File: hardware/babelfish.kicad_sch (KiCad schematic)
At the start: 103 parts, among them J1 Shifter Power, J2 SWD, J3 DE9 Female, J4 USB_A, Q1 BSS138, SW1 TS342A2P-WZ, SW2 TS342A2P-WZ, U1 RP2040, U10 DSWB04LHGET, U11 MAX3232IDR, U12 AP2191WG-7, U2 TPS2113ADRBR, U3 GT-USB-7010ASV, U4 W25Q128JVS, U6 TPMCP1703T-3302E_CB, U7 74HC4052PW,118, U8 74HC4052PW,118, U9 LMR14020SDDAR, X1 X322512MSB4SI

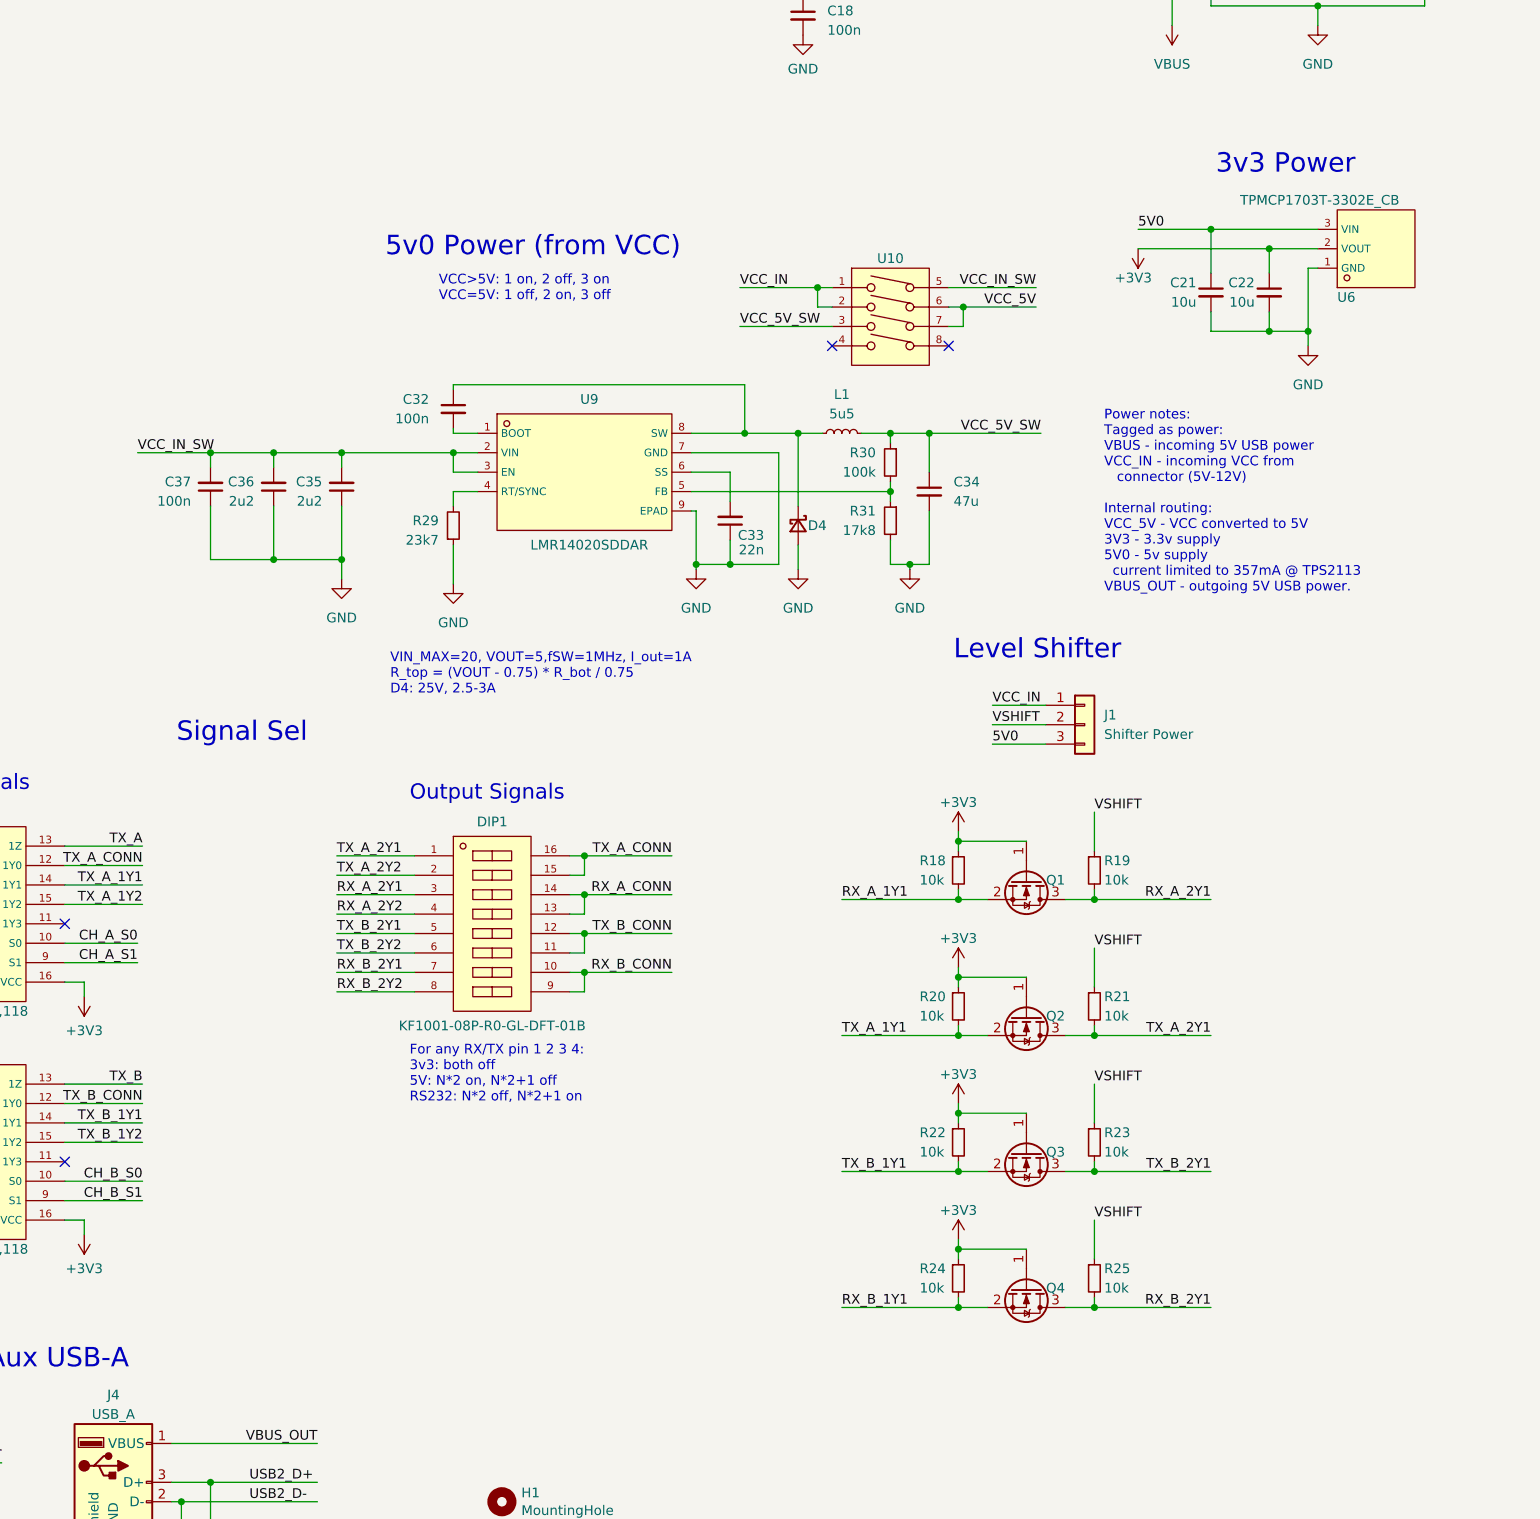
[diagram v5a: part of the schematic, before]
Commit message: Move 5V power to TPS62933, from WEBENCH
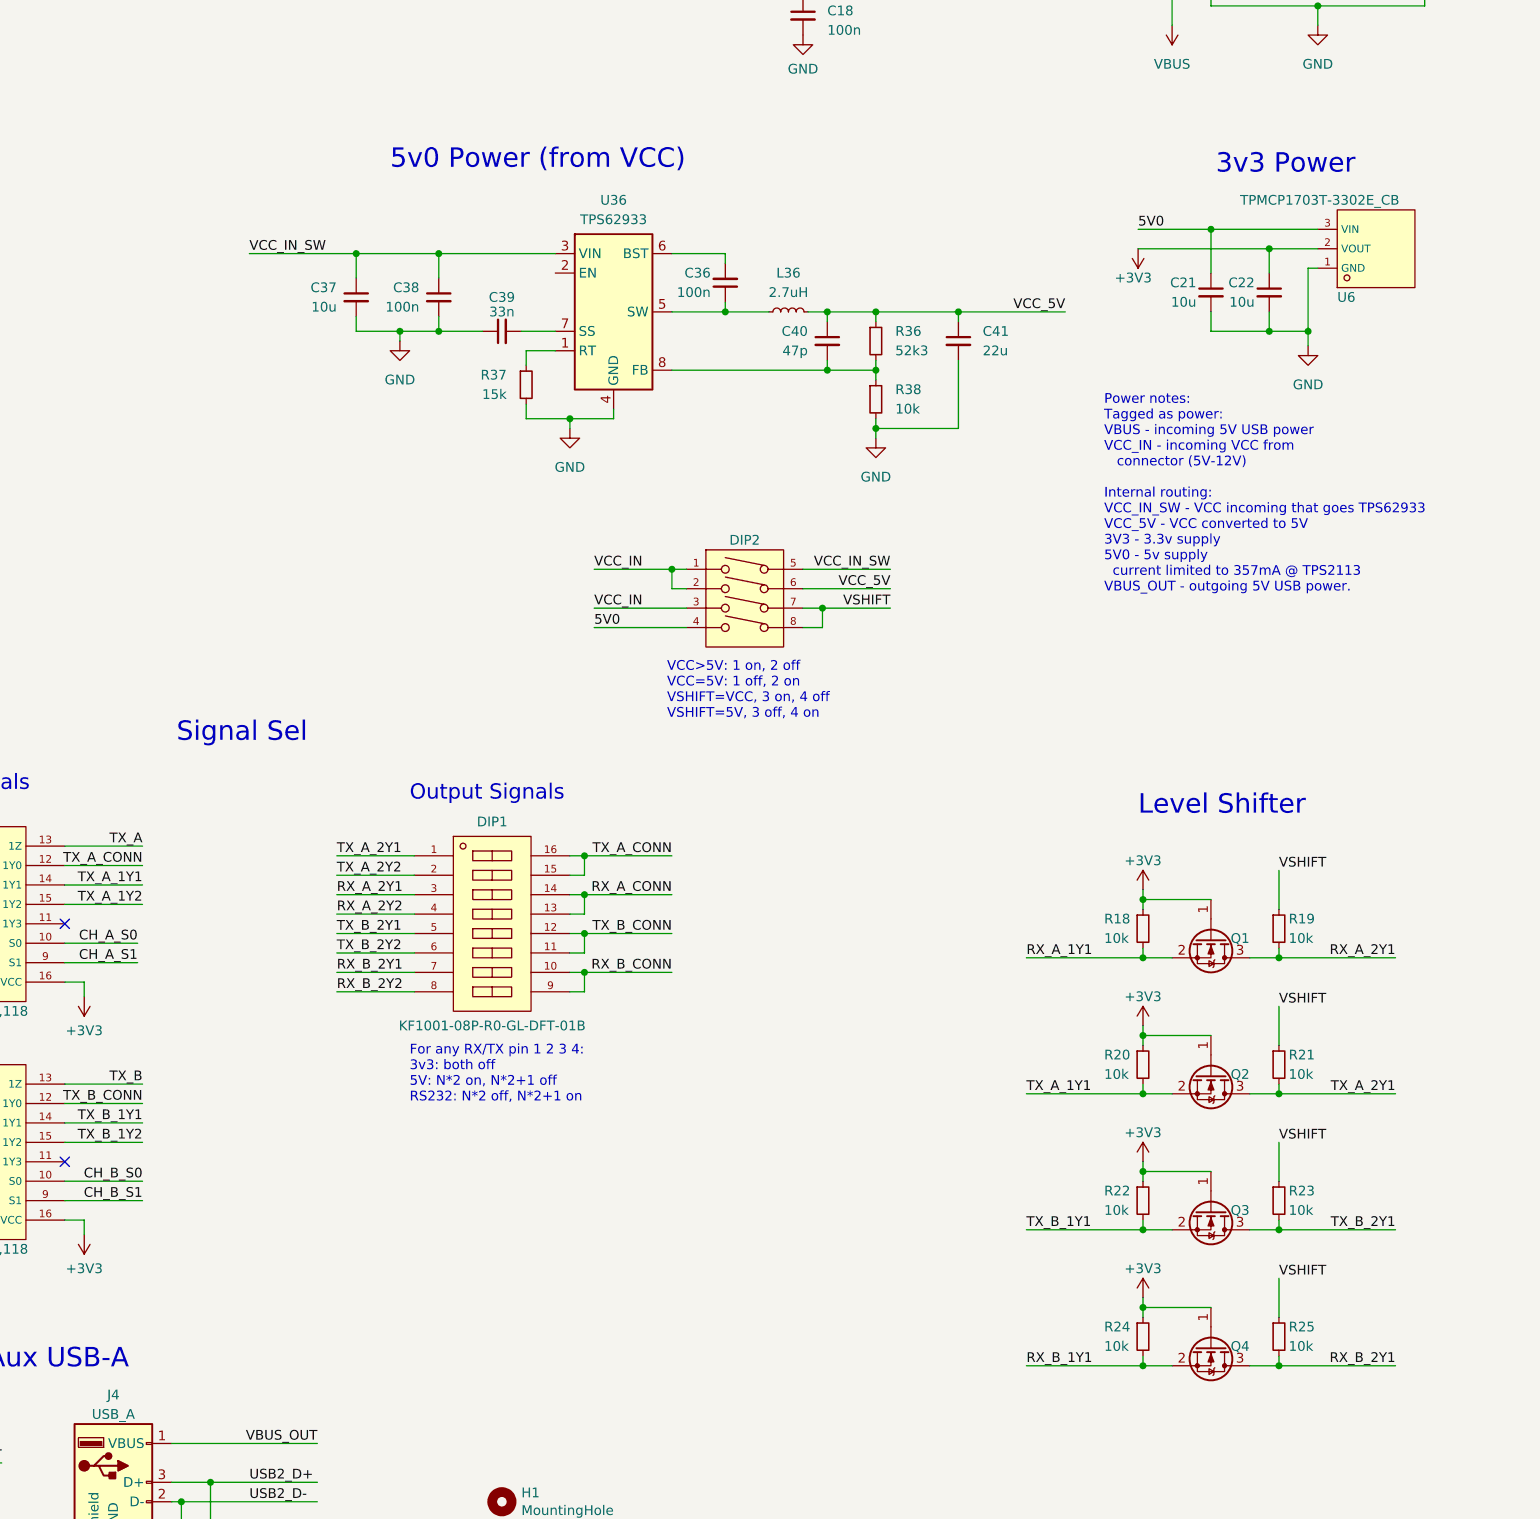
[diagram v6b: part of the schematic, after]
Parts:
- removed C32: 100n, Capacitor_SMD:C_0402_1005Metric, symbol Device:C_Small
- removed C33: 22n, Capacitor_SMD:C_0402_1005Metric, symbol Device:C_Small
- removed C34: 47u, Capacitor_SMD:C_0805_2012Metric, symbol Device:C_Small
- removed C35: 2u2, Capacitor_SMD:C_1206_3216Metric, symbol Device:C_Small
- removed D4: D_Schottky_Small, Diode_SMD:D_SMA, symbol Device:D_Schottky_Small
- removed J1: Shifter Power, Connector_PinHeader_2.54mm:PinHeader_1x03_P2.54mm_Vertical, symbol Connector_Generic:Conn_01x03
- removed L1: 5u5, symbol Device:L_Small
- removed R29: 23k7, symbol Device:R_Small
- removed R30: 100k, symbol Device:R_Small
- removed R31: 17k8, symbol Device:R_Small
- removed U9: LMR14020SDDAR, lcsc:HSOP-8_L5.0-W4.0-P1.27-LS6.2-BL-EP, symbol LCSC:LMR14020SDDAR
- added C38: 100n, Capacitor_SMD:C_0402_1005Metric, symbol Device:C_Small
- added C39: 33n, Capacitor_SMD:C_01005_0402Metric, symbol Device:C_Small
- added C40: 47p, Capacitor_SMD:C_0402_1005Metric, symbol Device:C_Small
- added C41: 22u, Capacitor_SMD:C_0805_2012Metric, symbol Device:C_Small
- added L36: 2.7uH, Inductor_SMD:L_12x12mm_H6mm, symbol Device:L_Small
- added R36: 52k3, Resistor_SMD:R_0402_1005Metric, symbol Device:R_Small
- added R37: 15k, Resistor_SMD:R_0402_1005Metric, symbol Device:R_Small
- added R38: 10k, Resistor_SMD:R_0402_1005Metric, symbol Device:R_Small
- added U36: TPS62933, Package_TO_SOT_SMD:SOT-583-8, symbol Regulator_Switching:TPS62933
- C36: value 2u2 -> 100n; footprint Capacitor_SMD:C_1206_3216Metric -> Capacitor_SMD:C_01005_0402Metric; ESR (none) -> 1mOhm; Notes X7R 100V -> (none)
- C37: value 100n -> 10u; footprint Capacitor_SMD:C_0402_1005Metric -> Capacitor_SMD:C_0805_2012Metric; ESR (none) -> 2.8mOhm; Notes X7R 100V -> (none)
- renumbered U10 to DIP2
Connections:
- net VCC_5V_SW is gone; now on net VCC_IN: DIP2.3
- net 5V0: now also DIP2.4
- net GND: now also C37.2, C38.2, C39.1, C41.2, R37.2, R38.2, U36.4 (GND); no longer C36.1, C37.1
- net VCC_5V: now also C40.1, C41.1, L36.2, R36.1; no longer DIP2.7
- net VCC_IN_SW: now also C37.1, C38.1, U36.3 (VIN); no longer C36.2, C37.2
- net VSHIFT: now also DIP2.7, DIP2.8
- new net: C40.2, R36.2, R38.1, U36.8 (FB)
- new net: R37.1, U36.1 (RT)
- new net: C36.1, L36.1, U36.5 (SW)
- new net: C39.2, U36.7 (SS)
- new net: C36.2, U36.6 (BST)
- no-connect marks 18 -> 16
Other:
- note added: "Power notes: Tagged as power: VBUS - incoming 5V USB power VCC_IN - incoming VCC from connector (5V-12V) Internal routing: VCC_IN_SW - VCC incoming that goes TPS62933 VCC_5V - VCC converted to 5V 3V3 - 3.3v supply 5V0 - 5v supply current limited to 357mA @ TPS2113 VBUS_OUT - outgoing 5V USB power."
- note added: "VCC>5V: 1 on, 2 off VCC=5V: 1 off, 2 on VSHIFT=VCC, 3 on, 4 off VSHIFT=5V, 3 off, 4 on"
- note removed: "Power notes: Tagged as power: VBUS - incoming 5V USB power VCC_IN - incoming VCC from connector (5V-12V) Internal routing: VCC_5V - VCC converted to 5V 3V3 - 3.3v supply 5V0 - 5v supply current limited to 357mA @ TPS2113 VBUS_OUT - outgoing 5V USB power."
- note removed: "VCC>5V: 1 on, 2 off, 3 on VCC=5V: 1 off, 2 on, 3 off"
- note removed: "VIN_MAX=20, VOUT=5,fSW=1MHz, I_out=1A R_top = (VOUT - 0.75) * R_bot / 0.75 D4: 25V, 2.5-3A"
- moved on the sheet: DIP2, Q1, Q2, Q3, Q4, R18, R19, R20, R21, R22, R23, R24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

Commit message: WIP -- pre-shift-up
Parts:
- L36: footprint Inductor_SMD:L_12x12mm_H6mm -> lcsc:IND-SMD_L6.0-W6.0_FNR60XXS
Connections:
- no-connect marks 16 -> 17
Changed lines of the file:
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@@
   (no_connect (at 187.325 153.035))
   (no_connect (at 198.12 187.325))
+  (no_connect (at 287.655 102.235))
   (no_connect (at 187.325 150.495))
   (no_connect (at 198.12 218.44))
@@
       (effects (font (size 1.27 1.27)))
     )
-    (property "Footprint" "Inductor_SMD:L_12x12mm_H6mm" (at 318.135 107.315 0)
+    (property "Footprint" "lcsc:IND-SMD_L6.0-W6.0_FNR60XXS" (at 318.135 107.315 0)
       (effects (font (size 1.27 1.27)) hide)
     )
